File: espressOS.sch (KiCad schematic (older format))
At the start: 128 parts

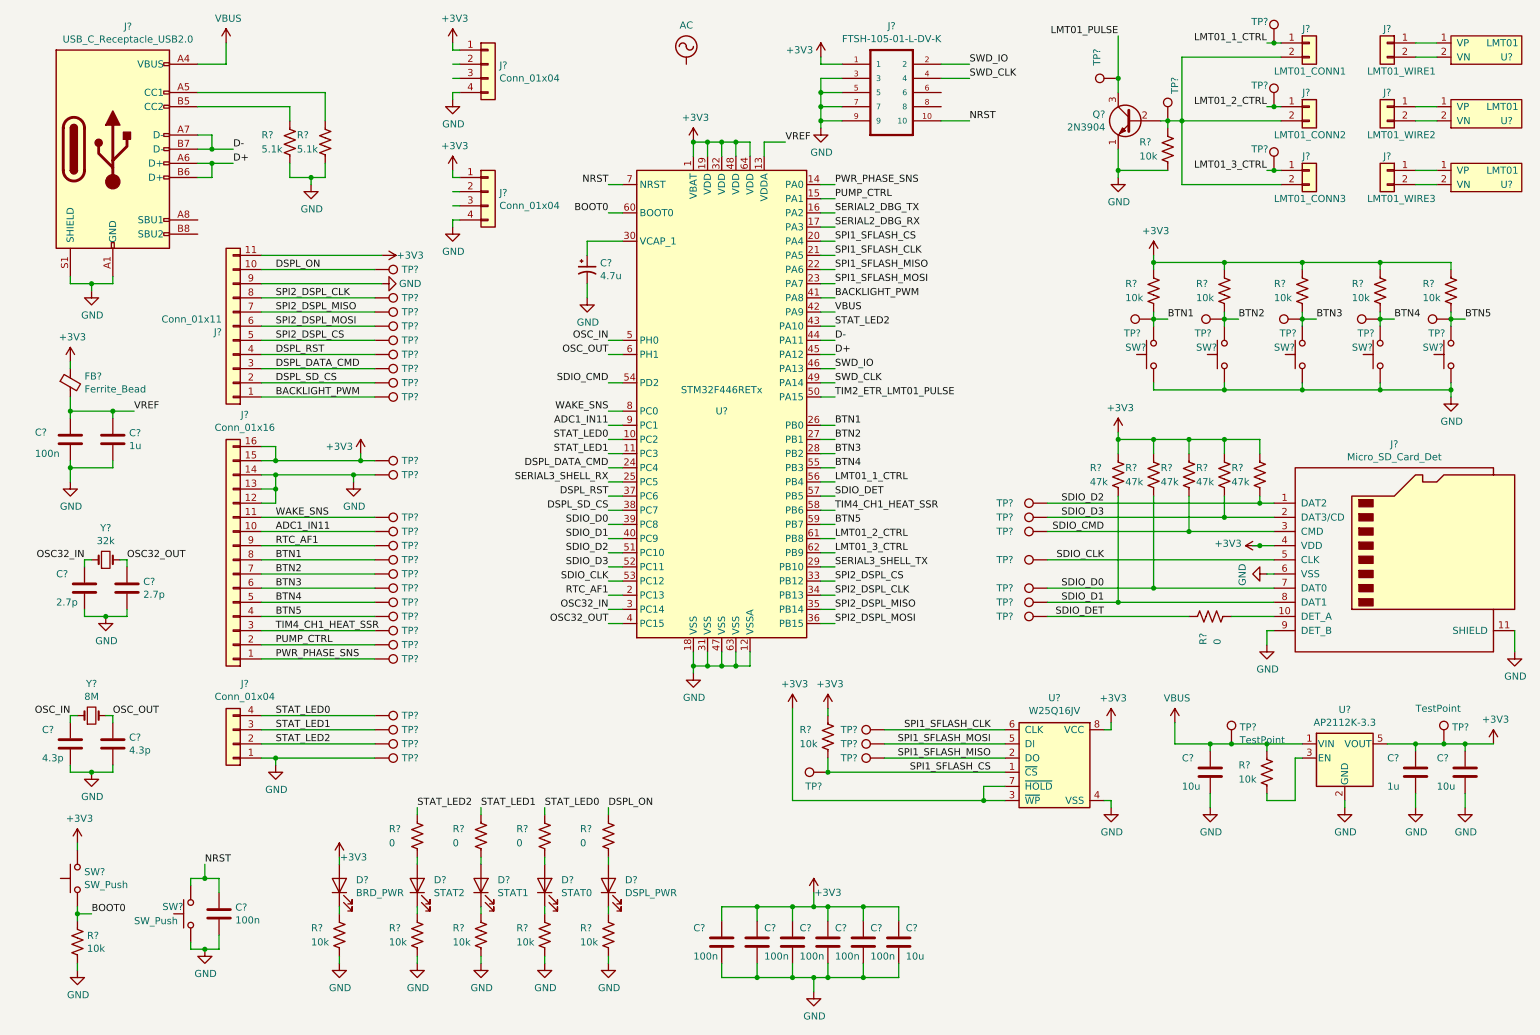
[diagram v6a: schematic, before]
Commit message: Update footprints
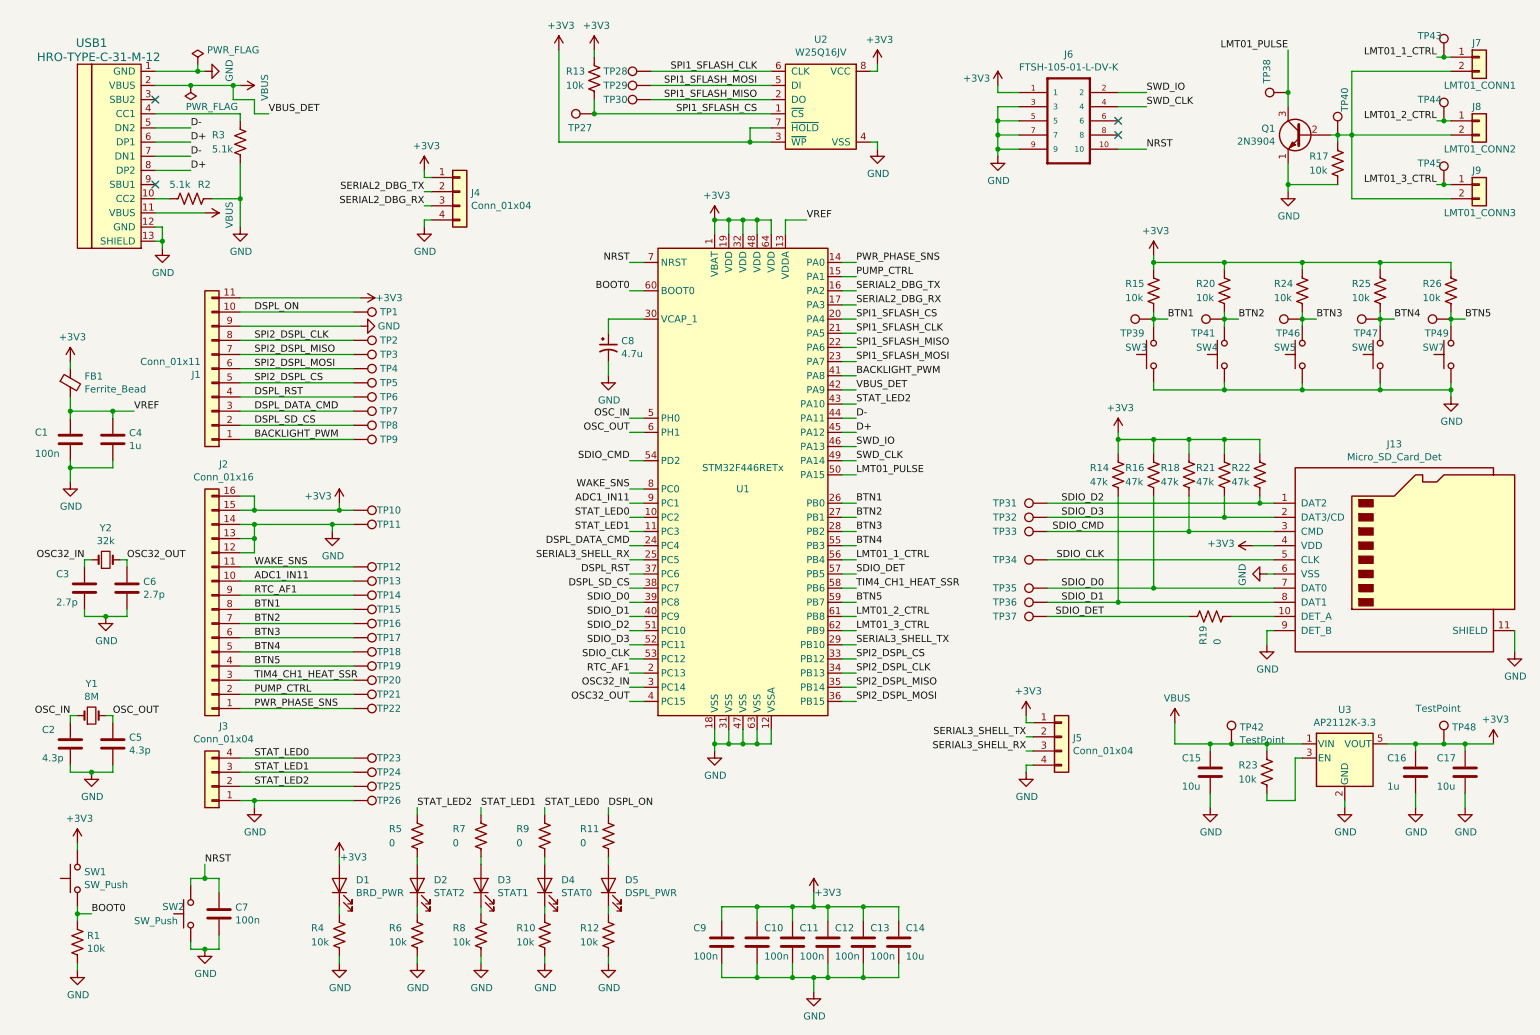
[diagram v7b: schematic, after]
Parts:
- removed J?: LMT01_WIRE1, symbol Connector_Generic:Conn_01x02
- removed J?: LMT01_WIRE2, symbol Connector_Generic:Conn_01x02
- removed J?: LMT01_WIRE3, symbol Connector_Generic:Conn_01x02
- removed J?: USB_C_Receptacle_USB2.0, symbol Connector:USB_C_Receptacle_USB2.0
- removed R?: 5.1k, symbol Device:R_US
- removed U? (x3): LMT01, symbol espressOS:LMT01
- added R3: 5.1k, symbol Device:R_US
- added USB1: HRO-TYPE-C-31-M-12, Type-C:USB_C_GCT_USB4085, symbol Type-C:HRO-TYPE-C-31-M-12
- J13: renamed from J?; footprint (none) -> Connector_Card:microSD_HC_Hirose_DM3D-SF
- J4, J5: renamed from J?; footprint (none) -> STEMMA-QT:JST_SM04B-SRSS-TB(LF)(SN)
- J7, J8, J9: renamed from J?; footprint (none) -> Connector_PinHeader_2.54mm:PinHeader_1x02_P2.54mm_Vertical
- gave numbers to parts that had none: 114
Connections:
- net TIM2_ETR_LMT01_PULSE is gone; now on net LMT01_PULSE: U1.50 (PA15)
- net D+: now also USB1.6 (DP1), USB1.8 (DP2)
- net D-: now also USB1.5 (DN2), USB1.7 (DN1)
- net GND: now also R2.1, R3.2, USB1.1 (GND), USB1.12 (GND), USB1.13 (SHIELD); no longer R2.2
- net SERIAL2_DBG_RX: now also J4.3 (Pin_3)
- net SERIAL2_DBG_TX: now also J4.2 (Pin_2)
- net SERIAL3_SHELL_RX: now also J5.3 (Pin_3)
- net SERIAL3_SHELL_TX: now also J5.2 (Pin_2)
- net VBUS: now also USB1.11 (VBUS), USB1.2 (VBUS)
- new net: R2.2, USB1.10 (CC2)
- new net: R3.1, USB1.4 (CC1)
- no-connect marks 0 -> 4
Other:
- moved on the sheet: C8, J1, J2, J3, J4, J5, J6, J7, J8, J9, Q1, R13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
